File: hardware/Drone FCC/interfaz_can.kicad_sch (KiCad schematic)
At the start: 16 parts, among them J801 CAN 1 Connector 1, J803 CAN 2 Connector 1, U801 SN65HVD230, U802 SN65HVD230

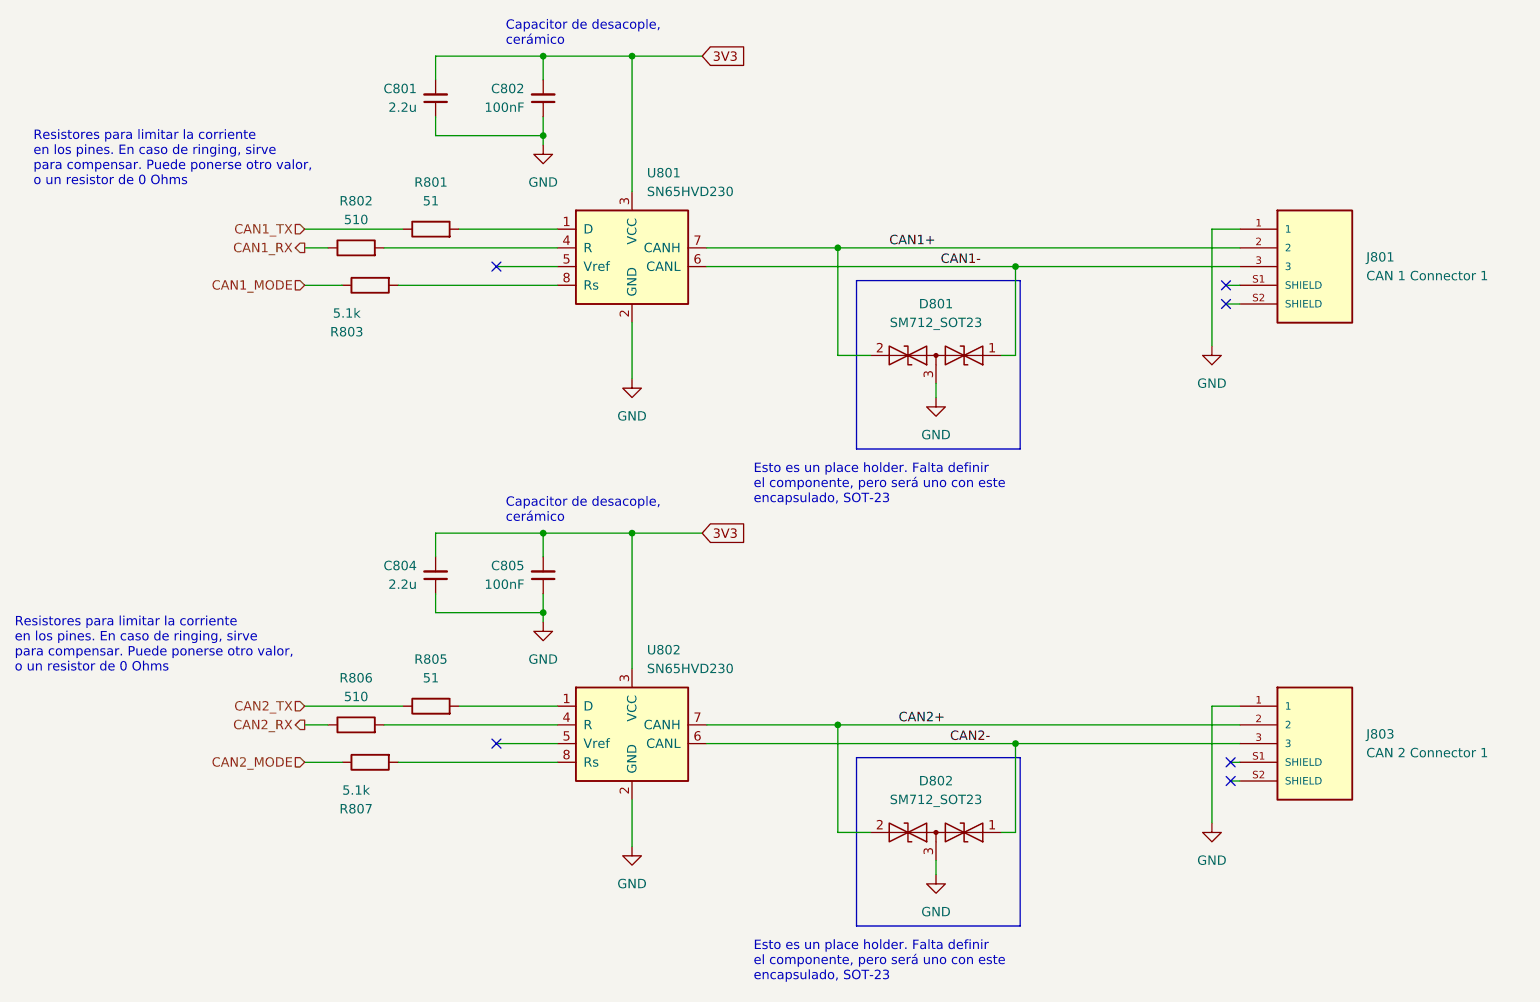
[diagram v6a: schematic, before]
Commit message: re routed everything with newer dimensions
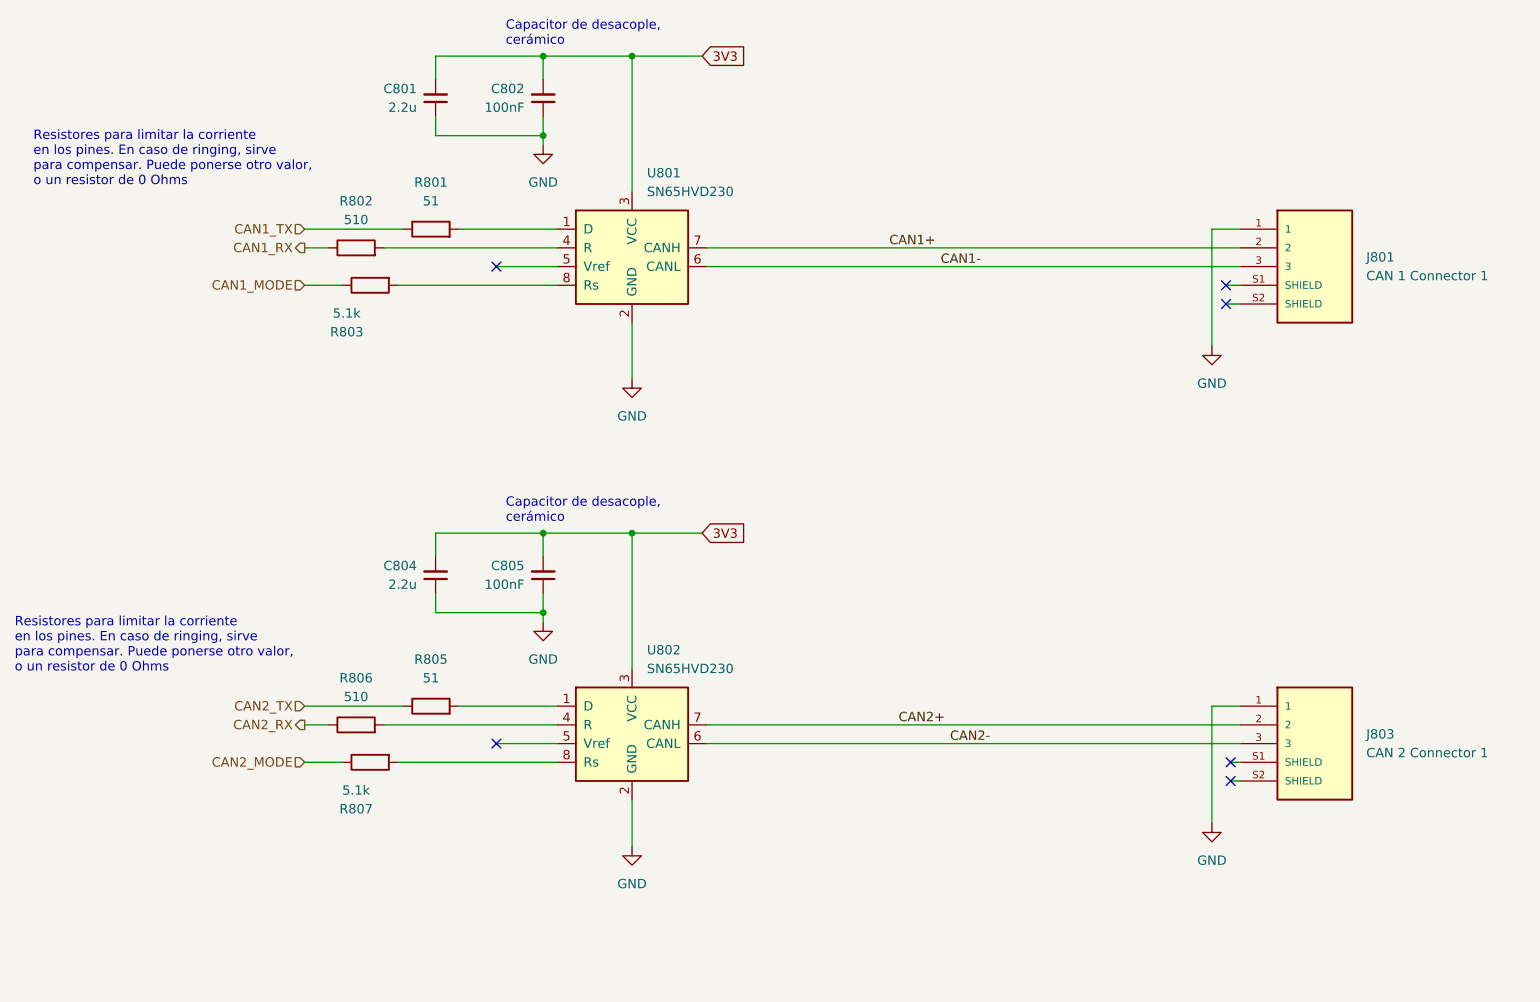
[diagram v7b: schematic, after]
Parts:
- removed D801, D802: SM712_SOT23, Package_TO_SOT_SMD:SOT-23, symbol Diode:SM712_SOT23
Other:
- note removed: "Esto es un place holder. Falta definir el componente, pero será uno con este encapsulado, SOT-23"
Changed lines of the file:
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@@
   (junction (at 145.415 26.035) (diameter 0) (color 0 0 0 0)
-  )
-  (junction (at 173.355 52.07) (diameter 0) (color 0 0 0 0)
-  )
-  (junction (at 173.355 116.84) (diameter 0) (color 0 0 0 0)
-  )
-  (junction (at 197.485 54.61) (diameter 0) (color 0 0 0 0)
-  )
-  (junction (at 197.485 119.38) (diameter 0) (color 0 0 0 0)
   )
   (junction (at 133.35 26.035) (diameter 0) (color 0 0 0 0)
@@
     (stroke (width 0) (type default) (color 0 0 0 0))
   )
-  (wire (pts (xy 197.485 119.38) (xy 227.965 119.38))
-    (stroke (width 0) (type default) (color 0 0 0 0))
-  )
   (wire (pts (xy 226.695 124.46) (xy 227.965 124.46))
     (stroke (width 0) (type default) (color 0 0 0 0))
@@
     (stroke (width 0) (type default) (color 0 0 0 0))
   )
-  (wire (pts (xy 173.355 116.84) (xy 227.965 116.84))
+  (wire (pts (xy 155.575 116.84) (xy 227.965 116.84))
     (stroke (width 0) (type default) (color 0 0 0 0))
   )
@@
     (stroke (width 0) (type default) (color 0 0 0 0))
   )
-  (wire (pts (xy 186.69 70.485) (xy 186.69 72.39))
-    (stroke (width 0) (type default) (color 0 0 0 0))
-  )
-  (wire (pts (xy 197.485 54.61) (xy 197.485 66.675))
-    (stroke (width 0) (type default) (color 0 0 0 0))
-  )
-  (polyline (pts (xy 198.12 56.515) (xy 198.12 79.375))
-    (stroke (width 0) (type default) (color 0 0 0 0))
-  )
   (wire (pts (xy 127 119.38) (xy 135.255 119.38))
     (stroke (width 0) (type default) (color 0 0 0 0))
   )
-  (polyline (pts (xy 175.895 121.285) (xy 198.12 121.285))
-    (stroke (width 0) (type default) (color 0 0 0 0))
-  )
   (wire (pts (xy 121.92 49.53) (xy 135.255 49.53))
     (stroke (width 0) (type default) (color 0 0 0 0))
@@
     (stroke (width 0) (type default) (color 0 0 0 0))
   )
-  (wire (pts (xy 186.69 135.255) (xy 186.69 137.16))
-    (stroke (width 0) (type default) (color 0 0 0 0))
-  )
   (wire (pts (xy 145.415 26.035) (xy 145.415 44.45))
     (stroke (width 0) (type default) (color 0 0 0 0))
@@
     (stroke (width 0) (type default) (color 0 0 0 0))
   )
-  (wire (pts (xy 155.575 52.07) (xy 173.355 52.07))
+  (wire (pts (xy 155.575 52.07) (xy 227.965 52.07))
     (stroke (width 0) (type default) (color 0 0 0 0))
   )
@@
     (stroke (width 0) (type default) (color 0 0 0 0))
   )
-  (wire (pts (xy 197.485 131.445) (xy 195.58 131.445))
-    (stroke (width 0) (type default) (color 0 0 0 0))
-  )
   (wire (pts (xy 100.965 49.53) (xy 114.3 49.53))
     (stroke (width 0) (type default) (color 0 0 0 0))
@@
     (stroke (width 0) (type default) (color 0 0 0 0))
   )
-  (wire (pts (xy 173.355 131.445) (xy 173.355 116.84))
-    (stroke (width 0) (type default) (color 0 0 0 0))
-  )
-  (wire (pts (xy 155.575 54.61) (xy 197.485 54.61))
-    (stroke (width 0) (type default) (color 0 0 0 0))
-  )
-  (polyline (pts (xy 175.895 56.515) (xy 198.12 56.515))
-    (stroke (width 0) (type default) (color 0 0 0 0))
-  )
-  (wire (pts (xy 177.8 131.445) (xy 173.355 131.445))
-    (stroke (width 0) (type default) (color 0 0 0 0))
-  )
   (wire (pts (xy 224.155 114.3) (xy 224.155 130.175))
     (stroke (width 0) (type default) (color 0 0 0 0))
@@
     (stroke (width 0) (type default) (color 0 0 0 0))
   )
-  (wire (pts (xy 155.575 119.38) (xy 197.485 119.38))
+  (wire (pts (xy 155.575 119.38) (xy 227.965 119.38))
     (stroke (width 0) (type default) (color 0 0 0 0))
   )
@@
     (stroke (width 0) (type default) (color 0 0 0 0))
   )
-  (wire (pts (xy 173.355 66.675) (xy 173.355 52.07))
-    (stroke (width 0) (type default) (color 0 0 0 0))
-  )
-  (wire (pts (xy 197.485 54.61) (xy 227.965 54.61))
-    (stroke (width 0) (type default) (color 0 0 0 0))
-  )
-  (polyline (pts (xy 175.895 121.285) (xy 175.895 144.145))
+  (wire (pts (xy 155.575 54.61) (xy 227.965 54.61))
     (stroke (width 0) (type default) (color 0 0 0 0))
   )
@@
     (stroke (width 0) (type default) (color 0 0 0 0))
   )
-  (polyline (pts (xy 198.12 144.145) (xy 175.895 144.145))
-    (stroke (width 0) (type default) (color 0 0 0 0))
-  )
   (wire (pts (xy 118.745 99.06) (xy 118.745 101.6))
     (stroke (width 0) (type default) (color 0 0 0 0))
   )
-  (wire (pts (xy 197.485 66.675) (xy 195.58 66.675))
-    (stroke (width 0) (type default) (color 0 0 0 0))
-  )
   (wire (pts (xy 111.76 52.07) (xy 135.255 52.07))
     (stroke (width 0) (type default) (color 0 0 0 0))
@@
     (stroke (width 0) (type default) (color 0 0 0 0))
   )
-  (wire (pts (xy 173.355 52.07) (xy 227.965 52.07))
-    (stroke (width 0) (type default) (color 0 0 0 0))
-  )
   (wire (pts (xy 127 54.61) (xy 135.255 54.61))
     (stroke (width 0) (type default) (color 0 0 0 0))
@@
     (stroke (width 0) (type default) (color 0 0 0 0))
   )
-  (polyline (pts (xy 198.12 79.375) (xy 175.895 79.375))
-    (stroke (width 0) (type default) (color 0 0 0 0))
-  )
   (wire (pts (xy 224.155 114.3) (xy 227.965 114.3))
     (stroke (width 0) (type default) (color 0 0 0 0))
@@
     (stroke (width 0) (type default) (color 0 0 0 0))
   )
-  (wire (pts (xy 177.8 66.675) (xy 173.355 66.675))
-    (stroke (width 0) (type default) (color 0 0 0 0))
-  )
-  (wire (pts (xy 155.575 116.84) (xy 173.355 116.84))
-    (stroke (width 0) (type default) (color 0 0 0 0))
-  )
-  (polyline (pts (xy 175.895 56.515) (xy 175.895 79.375))
-    (stroke (width 0) (type default) (color 0 0 0 0))
-  )
-  (polyline (pts (xy 198.12 121.285) (xy 198.12 144.145))
-    (stroke (width 0) (type default) (color 0 0 0 0))
-  )
   (wire (pts (xy 226.695 121.92) (xy 227.965 121.92))
     (stroke (width 0) (type default) (color 0 0 0 0))
@@
     (stroke (width 0) (type default) (color 0 0 0 0))
   )
-  (wire (pts (xy 197.485 119.38) (xy 197.485 131.445))
-    (stroke (width 0) (type default) (color 0 0 0 0))
-  )
   (wire (pts (xy 227.965 49.53) (xy 224.155 49.53))
     (stroke (width 0) (type default) (color 0 0 0 0))
   )
-  (text "Esto es un place holder. Falta definir\nel componente, pero será uno con este\nencapsulado, SOT-23"
-    (at 161.925 151.765 0)
-    (effects (font (size 1.27 1.27)) (justify left bottom))
-  )
   (text "Capacitor de desacople,\ncerámico" (at 128.27 24.765 0)
     (effects (font (size 1.27 1.27)) (justify left bottom))
   )
   (text "Capacitor de desacople,\ncerámico" (at 128.27 89.535 0)
-    (effects (font (size 1.27 1.27)) (justify left bottom))
-  )
-  (text "Esto es un place holder. Falta definir\nel componente, pero será uno con este\nencapsulado, SOT-23"
-    (at 161.925 86.995 0)
     (effects (font (size 1.27 1.27)) (justify left bottom))
   )
@@
     (pin "1")
   )
-  (symbol (lib_id "Diode:SM712_SOT23") (at 186.69 66.675 0) (mirror y) (unit 1)
-    (in_bom yes) (on_board yes) (fields_autoplaced)
-    (property "Reference" "D801" (id 0) (at 186.69 59.69 0))
-    (property "Value" "SM712_SOT23" (id 1) (at 186.69 62.23 0))
-    (property "Footprint" "Package_TO_SOT_SMD:SOT-23" (id 2) (at 186.69 75.565 0)
-      (effects (font (size 1.27 1.27)) hide)
-    )
-    (property "Datasheet" "https://www.littelfuse.com/~/media/electronics/datasheets/tvs_diode_arrays/littelfuse_tvs_diode_array_sm712_datasheet.pdf.pdf" (id 3) (at 190.5 66.675 0)
-      (effects (font (size 1.27 1.27)) hide)
-    )
-    (pin "1")
-    (pin "2")
-    (pin "3")
-  )
   (symbol (lib_id "DF13A-3P-1.25H(21):HRS_DF13A-3P-1.25H(21)") (at 236.855 137.16 0) (unit 1)
     (in_bom yes) (on_board yes) (fields_autoplaced)
@@
     (pin "2")
   )
-  (symbol (lib_id "Diode:SM712_SOT23") (at 186.69 131.445 0) (mirror y) (unit 1)
-    (in_bom yes) (on_board yes) (fields_autoplaced)
-    (property "Reference" "D802" (id 0) (at 186.69 124.46 0))
-    (property "Value" "SM712_SOT23" (id 1) (at 186.69 127 0))
-    (property "Footprint" "Package_TO_SOT_SMD:SOT-23" (id 2) (at 186.69 140.335 0)
-      (effects (font (size 1.27 1.27)) hide)
-    )
-    (property "Datasheet" "https://www.littelfuse.com/~/media/electronics/datasheets/tvs_diode_arrays/littelfuse_tvs_diode_array_sm712_datasheet.pdf.pdf" (id 3) (at 190.5 131.445 0)
-      (effects (font (size 1.27 1.27)) hide)
-    )
-    (pin "1")
-    (pin "2")
-    (pin "3")
-  )
-  (symbol (lib_name "GND_2") (lib_id "power:GND") (at 186.69 72.39 0) (unit 1)
-    (in_bom yes) (on_board yes) (fields_autoplaced)
-    (property "Reference" "#PWR0135" (id 0) (at 186.69 78.74 0)
-      (effects (font (size 1.27 1.27)) hide)
-    )
-    (property "Value" "GND" (id 1) (at 186.69 77.47 0))
-    (property "Footprint" "" (id 2) (at 186.69 72.39 0)
-      (effects (font (size 1.27 1.27)) hide)
-    )
-    (property "Datasheet" "" (id 3) (at 186.69 72.39 0)
-      (effects (font (size 1.27 1.27)) hide)
-    )
-    (pin "1")
-  )
-  (symbol (lib_name "GND_2") (lib_id "power:GND") (at 186.69 137.16 0) (unit 1)
-    (in_bom yes) (on_board yes) (fields_autoplaced)
-    (property "Reference" "#PWR0134" (id 0) (at 186.69 143.51 0)
-      (effects (font (size 1.27 1.27)) hide)
-    )
-    (property "Value" "GND" (id 1) (at 186.69 142.24 0))
-    (property "Footprint" "" (id 2) (at 186.69 137.16 0)
-      (effects (font (size 1.27 1.27)) hide)
-    )
-    (property "Datasheet" "" (id 3) (at 186.69 137.16 0)
-      (effects (font (size 1.27 1.27)) hide)
-    )
-    (pin "1")
-  )
   (symbol (lib_name "GND_2") (lib_id "power:GND") (at 224.155 65.405 0) (unit 1)
